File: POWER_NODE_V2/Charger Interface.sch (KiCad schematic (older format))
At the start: 0 parts

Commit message: WIP
making good progress
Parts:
- added C? (x4): 200 nF / 50V / SMD 0603, symbol C
- added J? (x2): CONN_01X04, symbol CONN_01X04
- added R? (x4): 2K / .1 W / 1% / SMD 0603, symbol R
- added R? (x4): 10K / .1 W / 1% / SMD 0603, symbol R
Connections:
- new net: J?.1 (P1), R?.1, R?.1 (x2)
- new net: J?.2 (P2), R?.1, R?.1 (x2)
- new net +5V: J?.4 (P4), J?.4 (P4)
- new net BATT_I: C?.1, R?.2
- new net BATT_I_REF: C?.1, R?.2
- new net CHG_I: C?.1, R?.2
- new net CHG_I_REF: C?.1, R?.2
- new net GND: C?.2, C?.2, C?.2, C?.2, J?.3 (P3), J?.3 (P3), R?.2, R?.2, R?.2, R?.2

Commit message: WIP
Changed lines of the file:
@@
 $EndComp
 Wire Wire Line
-	1300 1850 1500 1850
-Wire Wire Line
-	1500 1850 1800 1850
+	1300 1850 1800 1850
 Wire Wire Line
 	1500 1850 1500 2050
 Connection ~ 1500 1850
 Wire Wire Line
-	2100 1850 3100 1850
-Wire Wire Line
-	3100 1850 4500 1850
+	2100 1850 4500 1850
 Wire Wire Line
 	3100 1850 3100 2000
 Wire Wire Line
-	1300 950  1500 950
-Wire Wire Line
-	1500 950  1850 950
+	1300 950  1850 950
 Wire Wire Line
 	1500 950  1500 1150
 Connection ~ 1500 950
 Wire Wire Line
-	2150 950  3100 950
-Wire Wire Line
-	3100 950  5200 950
+	2150 950  5200 950
 Wire Wire Line
 	3100 1150 3100 950
@@
 $EndComp
 Wire Wire Line
-	1250 3650 1450 3650
-Wire Wire Line
-	1450 3650 1800 3650
+	1250 3650 1800 3650
 Wire Wire Line
 	1450 3650 1450 3850
 Connection ~ 1450 3650
 Wire Wire Line
-	2100 3650 3050 3650
-Wire Wire Line
-	3050 3650 4450 3650
+	2100 3650 4450 3650
 Wire Wire Line
 	3050 3650 3050 3800
 Wire Wire Line
-	1250 2850 1450 2850
-Wire Wire Line
-	1450 2850 1800 2850
+	1250 2850 1800 2850
 Wire Wire Line
 	1450 2850 1450 2950
 Connection ~ 1450 2850
 Wire Wire Line
-	2100 2850 3050 2850
-Wire Wire Line
-	3050 2850 5200 2850
+	2100 2850 5200 2850
 Wire Wire Line
 	3050 2950 3050 2850

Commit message: more WIP
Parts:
- added C? (x4): 100nF / 50V / 10% / SMD 0603, symbol C
- added D?: BAS16, symbol D
- added D?: D, symbol D
- added D?: EL-17-21VGC/TR8, symbol LED
- added J? (x3): CONN_01X02, symbol CONN_01X02
- added R?: 50 / .1 W / 10% / SMD 0603, symbol R
- added R?: 4.7k / .1 W / 10% / SMD 0603, symbol R
- added R? (x2): 82R0 / 0.25W / 1% / SMD 0805, symbol R
- added R? (x2): 220R / 0.25W / 1% / SMD 0805, symbol R
- added R? (x2): 300K / 0.5W / 1% / SMD 1206, symbol R
- added R? (x2): 1K / 0.75W / 5% / 400V / SMD 2010, symbol R
- added R? (x2): 1K0 / 0.063W / 1% / SMD 0603, symbol R
- added R? (x2): R, symbol R
- added U?: RTE24024, symbol RTE24024
- added U?: NUD3124LT1G, symbol NUD3124LT1G
- added U? (x2): TL783CKTTR, symbol TL783CKTTR
- added U? (x2): AMC1100DWV, symbol AMC1100DWV
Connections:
- net BATT_VOLT: now also R?.1
- net CHG_VOLT: now also R?.1
- net CHR_RLY: now also R?.2
- net GND: now also C?.1, C?.1, D?.2 (A), J?.2 (P2), R?.2, R?.2, R?.2, U?.2 (S(GND)), U?.5 (GND2), U?.5 (GND2)
- new net: D?.2 (A), U?.3 (D), U?.A2
- new net: D?.1 (K), D?.2 (A), J?.1 (P1), U?.14
- new net: R?.1, U?.1 (Gate)
- new net: D?.1 (K), R?.1
- new net: R?.1, R?.2, U?.1 (ADJ) (x2)
- new net: C?.2, R?.1, U?.1 (VDD1), U?.2 (OUT), U?.4 (OUT)
- new net: C?.1, R?.1, U?.1 (VDD1), U?.2 (OUT), U?.4 (OUT)
- new net: R?.1, R?.2, U?.2 (VINP) (x2)
- new net: R?.1, U?.6 (VOUTN) (x2)
- new net: R?.2, U?.7 (VOUTP) (x2)
- new net +24V: D?.1 (K), U?.11, U?.A1
- new net +3V3: C?.2, C?.2, U?.8 (VDD2), U?.8 (VDD2)
- new net BATT_N_HOT: C?.1, J?.2 (P2), R?.2, R?.2, U?.2 (VINP), U?.4 (GND1)
- new net BATT_P_HOT: J?.1 (P1), R?.1, U?.3 (IN)
- new net CHARGE_N_HOT: C?.2, J?.2 (P2), R?.1, R?.2, U?.2 (VINP), U?.4 (GND1)
- new net CHARGE_P_HOT: J?.1 (P1), R?.2, U?.3 (IN)
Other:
- note added: "Charger Relay\nMax 8A"
- moved on the sheet: C?, J?, R?

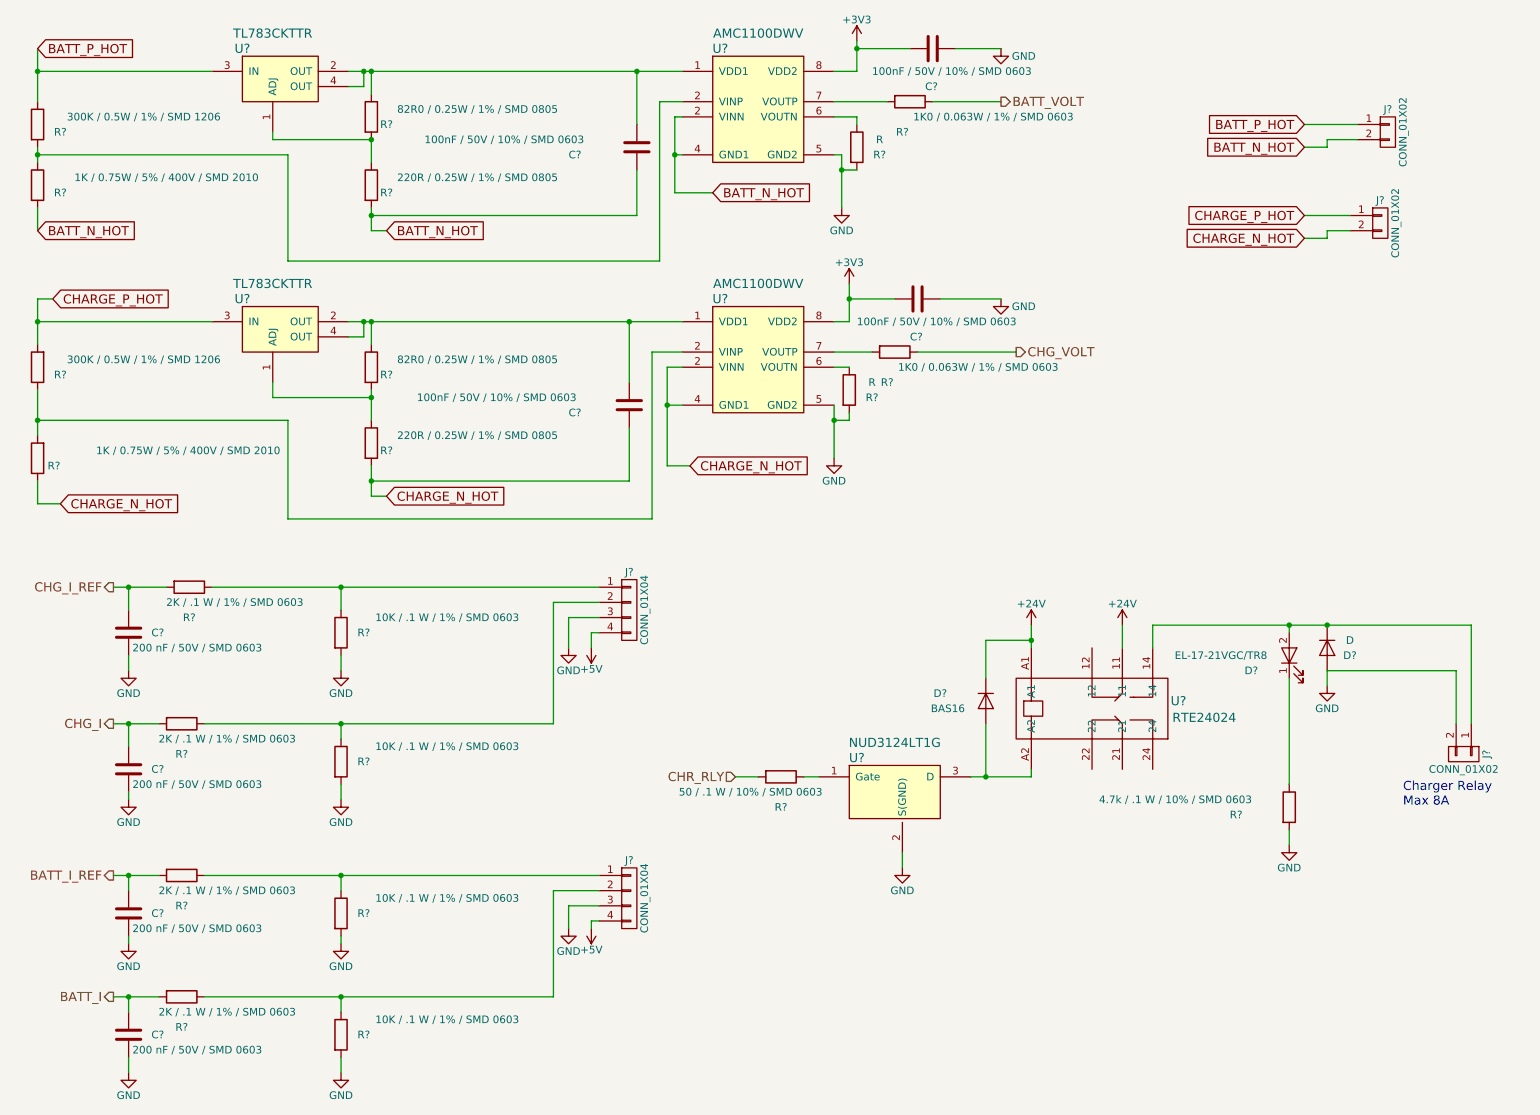
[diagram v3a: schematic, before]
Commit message: Schematic for Power Node V2 mostly done - mostly need connectors
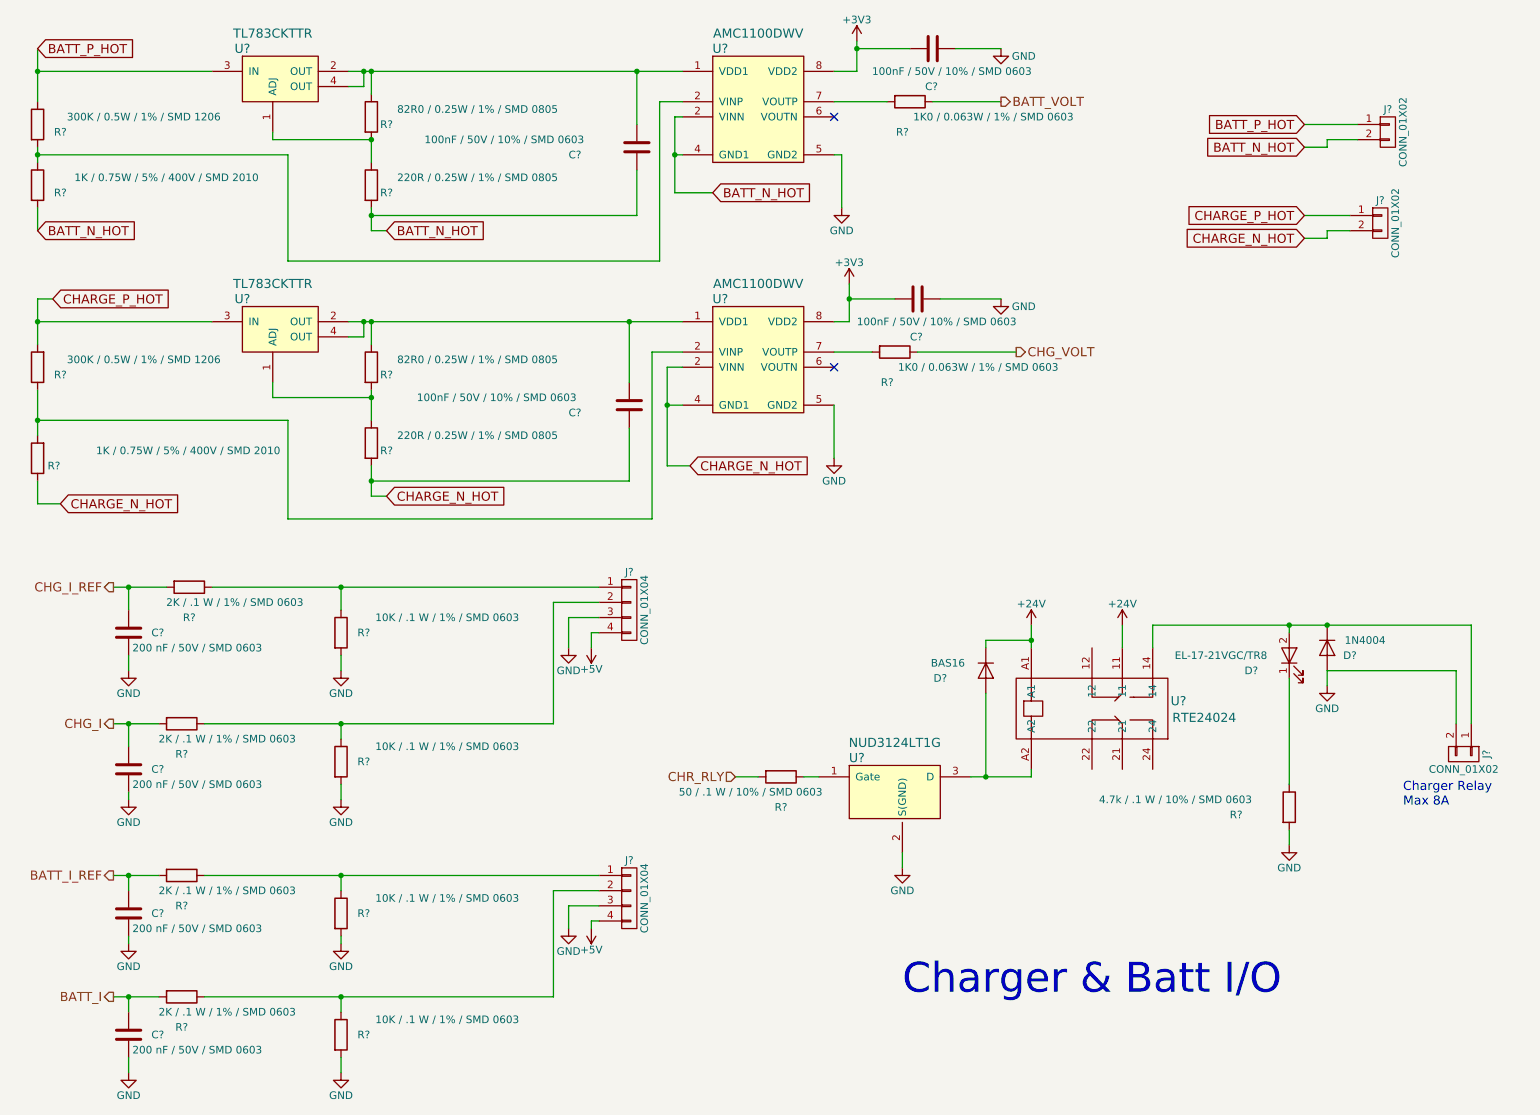
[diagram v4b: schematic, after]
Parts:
- removed R? (x2): R, symbol R
- D?: value D -> 1N4004
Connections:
- no-connect marks 0 -> 2
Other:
- note added: "Charger & Batt I/O"
- moved on the sheet: D?

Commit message: made a lot of footprints, began PCB layout for power node v2
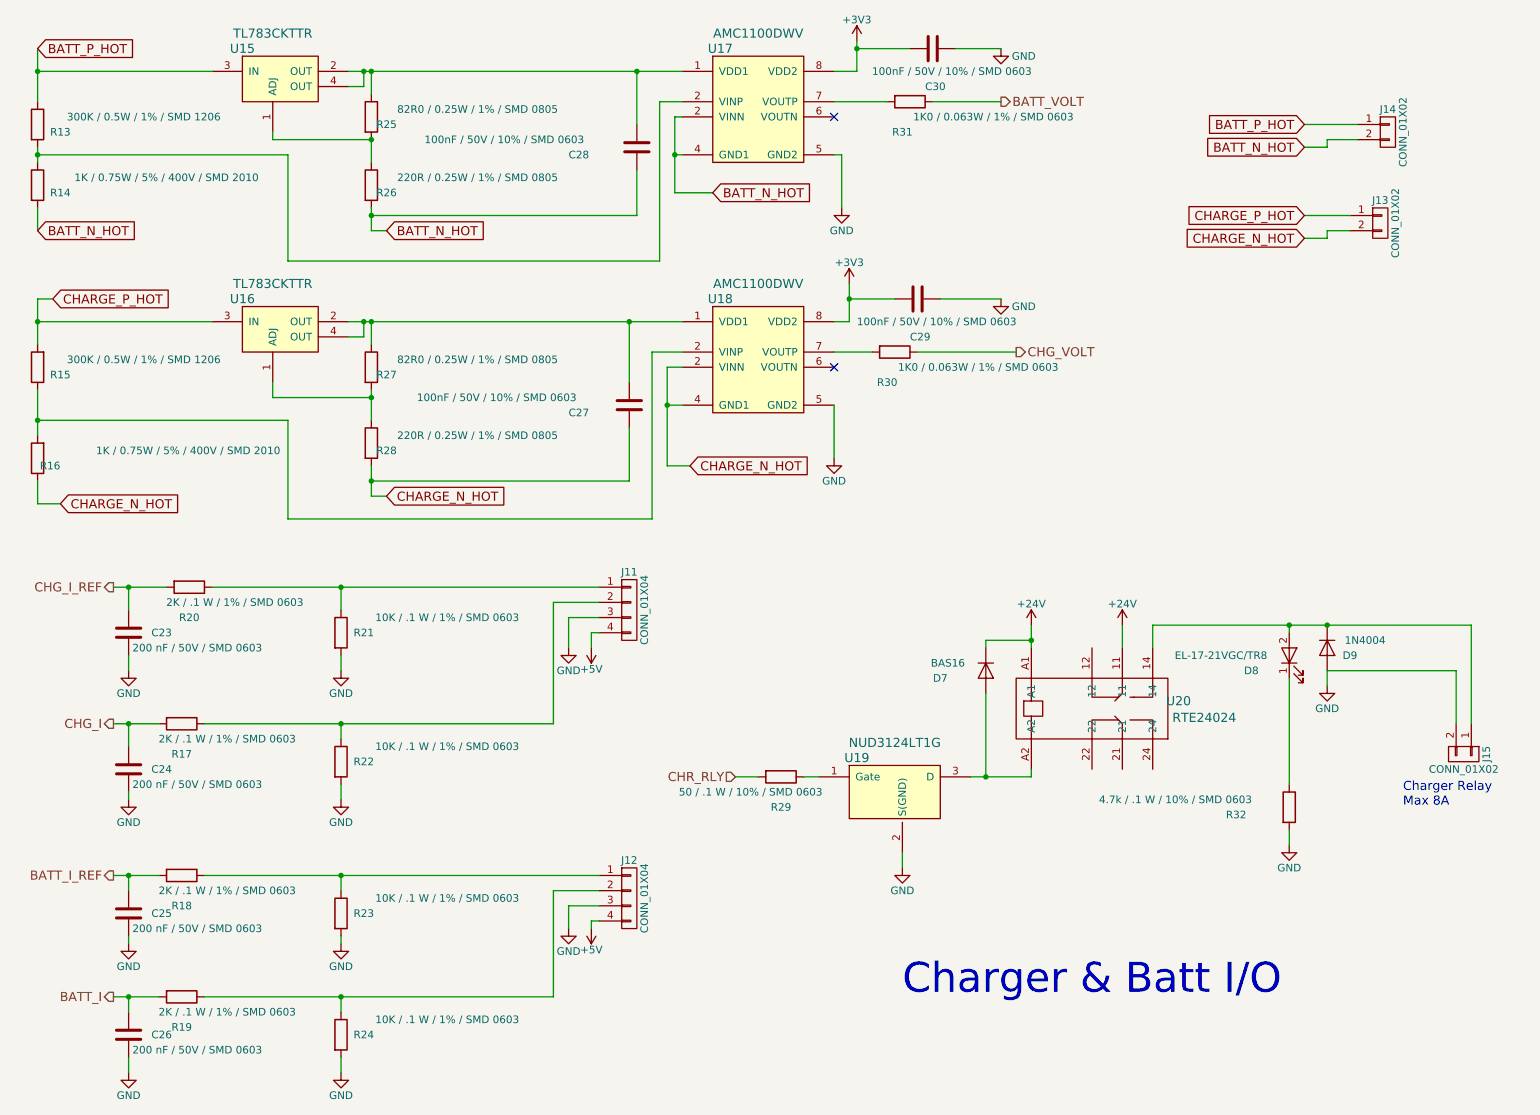
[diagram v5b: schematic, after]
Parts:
- C23, C24, C25, C26, C27, C28, C29, C30: renamed from C?; footprint (none) -> Capacitors_SMD:C_0603
- D7: renamed from D?; footprint (none) -> Diodes_SMD:D_SOT-23_ANK
- D8: renamed from D?; footprint (none) -> rLoop Footprints:LED_0805
- D9: renamed from D?; footprint (none) -> Diodes_THT:D_DO-201_P15.24mm_Horizontal
- J11, J12: renamed from J?; footprint (none) -> Pin_Headers:Pin_Header_Straight_1x04_Pitch2.54mm
- J13, J14, J15: renamed from J?; footprint (none) -> Pin_Headers:Pin_Header_Straight_1x02_Pitch2.54mm
- R13, R15: renamed from R?; footprint (none) -> Resistors_SMD:R_1206
- R14, R16: renamed from R?; footprint (none) -> Resistors_SMD:R_2010
- R17, R18, R19, R20, R21, R22, R23, R24, R29, R30, R31, R32: renamed from R?; footprint (none) -> Resistors_SMD:R_0603
- R25, R26, R27, R28: renamed from R?; footprint (none) -> Resistors_SMD:R_0805
- U15, U16: renamed from U?; footprint (none) -> TO_SOT_Packages_SMD:TO-263-3_TabPin2
- U17, U18: renamed from U?; footprint (none) -> rLoop Footprints:amc1100_SOIC8
- U19: renamed from U?; footprint (none) -> TO_SOT_Packages_SMD:SOT-23
- U20: renamed from U?; footprint (none) -> rLoop Footprints:RTE24024
